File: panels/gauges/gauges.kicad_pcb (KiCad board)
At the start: 2 copper layers, 190 x 100 mm, 0 parts

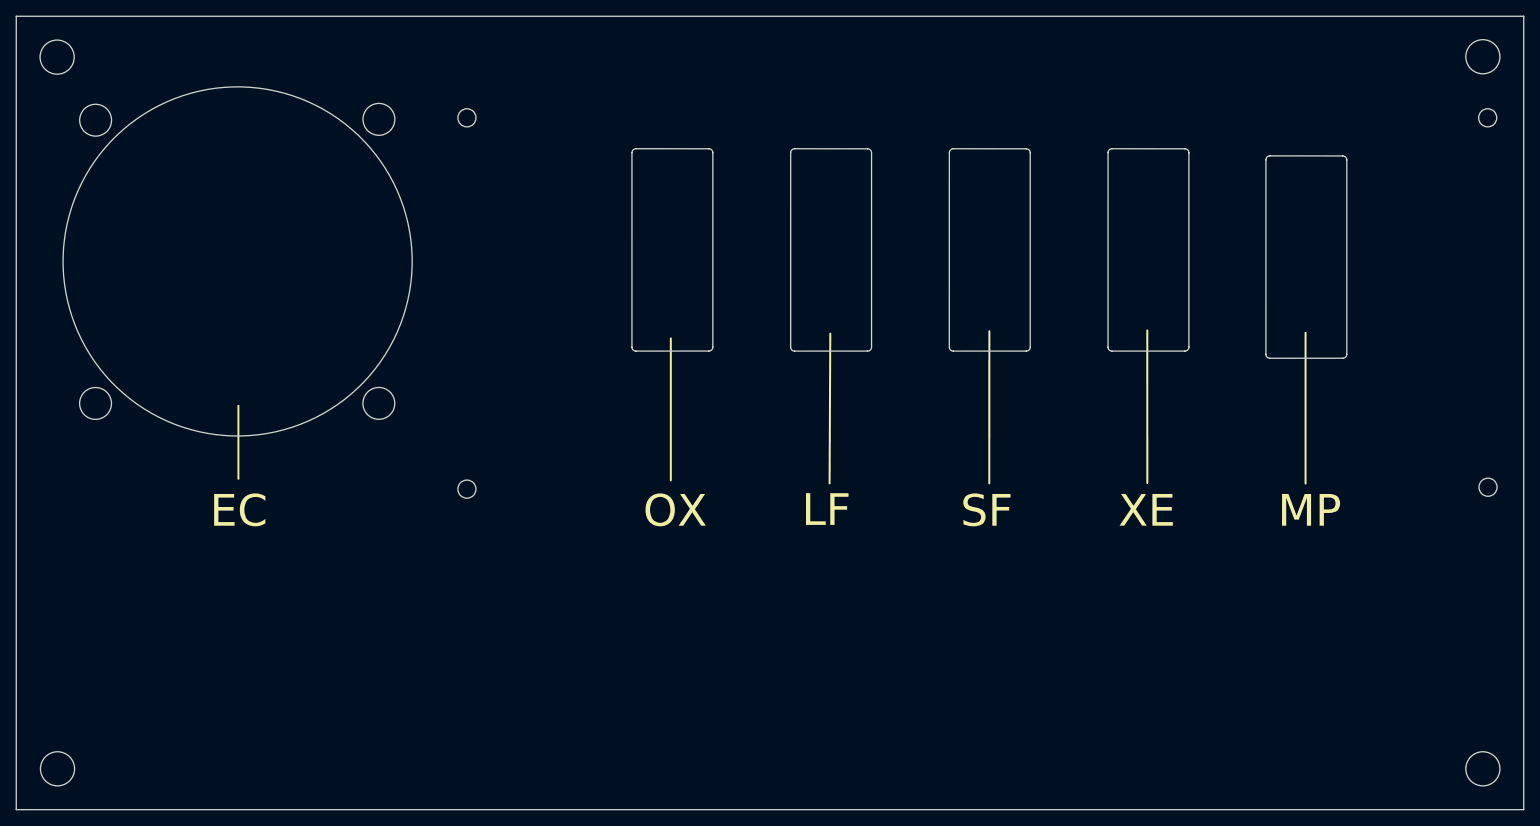
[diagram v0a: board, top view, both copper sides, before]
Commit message: panels: gauges=> aligned mounting holes
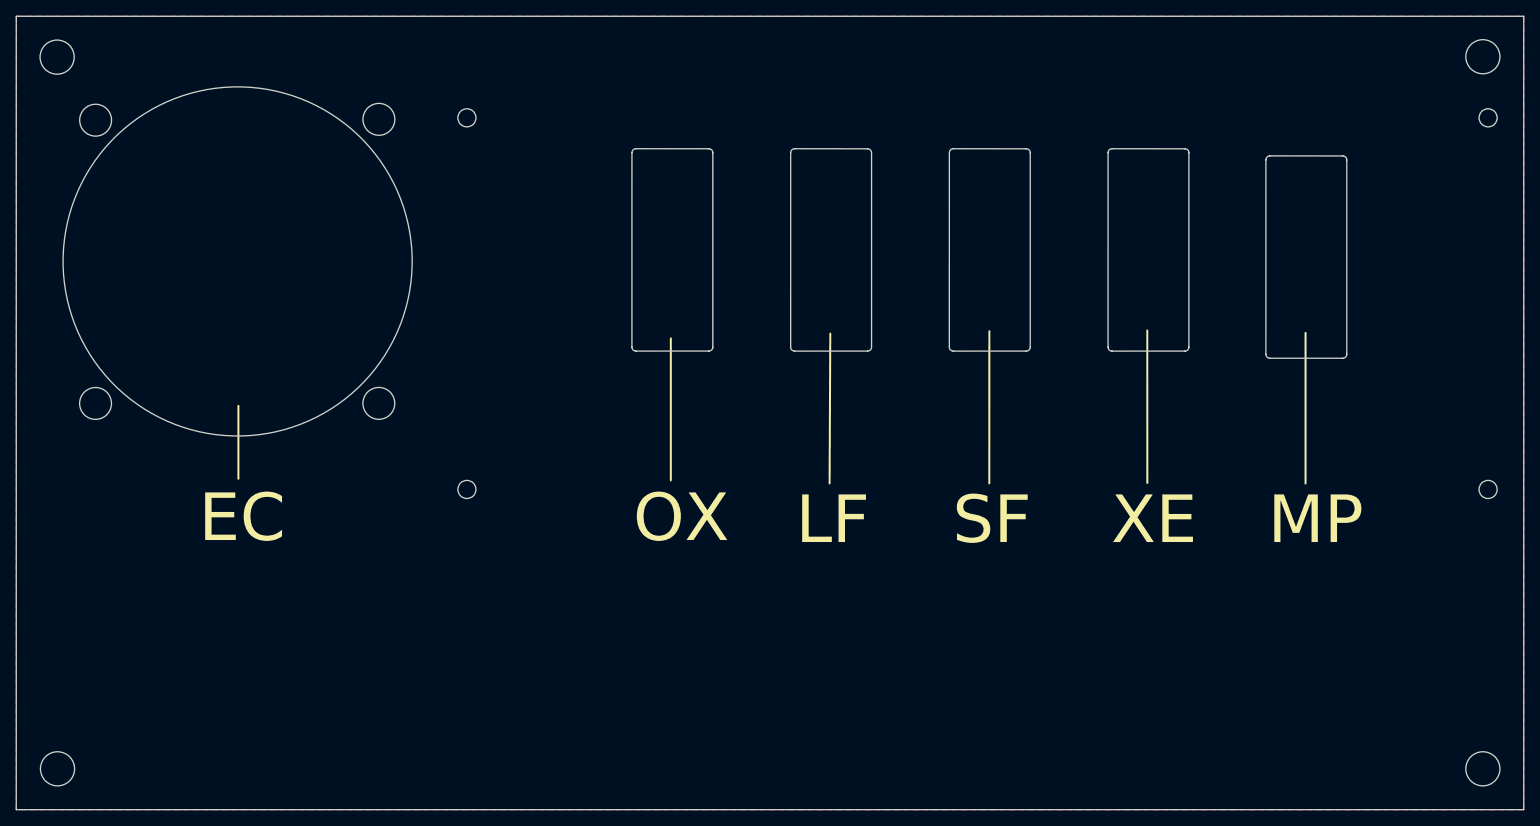
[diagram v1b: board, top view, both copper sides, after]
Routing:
- added copper zone on F.Cu, net (none)
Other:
- outline, holes or cut-outs redrawn
